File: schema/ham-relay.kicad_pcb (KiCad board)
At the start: 2 copper layers, 140 x 98 mm, 72 parts, among them J1 DB9, P1 JTAG, P2 CONN_01X08, P3 RESET, P4 ISP, P5 CONN_01X03, U1 REG3V3, U2 CPC1017N, U3 LPC1114FN28/102, U4 XYZ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

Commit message: Production ready
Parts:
- added HOLE2: 1pin, Connect:1pin, F.Cu at (183.3, 133.1)
- added HOLE2: 1pin, Connect:1pin, F.Cu at (75.3, 133.1)
- added HOLE2: 1pin, Connect:1pin, F.Cu at (75.3, 41.1)
- added HOLE2: 1pin, Connect:1pin, F.Cu at (183.3, 41.1)
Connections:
- J1 pad : (no net) -> GND
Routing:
- net GND: track 82.9 -> 97.2 mm
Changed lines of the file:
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@@
 (kicad_pcb (version 4) (host pcbnew 4.0.1-stable)
   (general
-    (links 163)
+    (links 169)
     (no_connects 0)
     (area 57.709999 38.024999 197.860001 136.175001)
     (thickness 1.6)
     (drawings 41)
-    (tracks 367)
+    (tracks 376)
     (zones 0)
-    (modules 72)
+    (modules 76)
     (nets 71)
   )
   (page A4)
   (layers
-    (0 F.Cu signal hide)
+    (0 F.Cu signal)
     (31 B.Cu signal)
     (32 B.Adhes user)
@@
     (mod_text_size 1 1)
     (mod_text_width 0.15)
-    (pad_size 3.35 3.35)
-    (pad_drill 3.048)
+    (pad_size 6 6)
+    (pad_drill 3.8)
     (pad_to_mask_clearance 0.2)
     (aux_axis_origin 69.342 125.222)
@@
     (add_net +12V)
   )
-  (module TO_SOT_Packages_THT:TO-220_Neutral123_Horizontal (layer F.Cu)
+  (module Connect:1pin (layer F.Cu)
+    (at 183.285 133.1)
+    (descr "module 1 pin (ou trou mecanique de percage)")
+    (tags DEV)
+    (zone_connect 2)
+    (fp_text reference HOLE2 (at 0 -3.048) (layer F.SilkS) hide
+      (effects (font (size 1 1) (thickness 0.15)))
+    )
+    (fp_text value 1pin (at 0 2.794) (layer F.Fab)
+      (effects (font (size 1 1) (thickness 0.15)))
+    )
+    (fp_circle (center 0 0) (end 0 -2.286) (layer F.SilkS) (width 0.15))
+    (pad 1 thru_hole circle (at 0 0) (size 6 6) (drill 3.8) (layers *.Cu *.Mask F.SilkS)
+      (net 1 GND) (zone_connect 2))
+  )
+  (module Connect:1pin (layer F.Cu)
+    (at 75.285 133.1)
+    (descr "module 1 pin (ou trou mecanique de percage)")
+    (tags DEV)
+    (zone_connect 2)
+    (fp_text reference HOLE2 (at 0 -3.048) (layer F.SilkS) hide
+      (effects (font (size 1 1) (thickness 0.15)))
+    )
+    (fp_text value 1pin (at 0 2.794) (layer F.Fab)
+      (effects (font (size 1 1) (thickness 0.15)))
+    )
+    (fp_circle (center 0 0) (end 0 -2.286) (layer F.SilkS) (width 0.15))
+    (pad 1 thru_hole circle (at 0 0) (size 6 6) (drill 3.8) (layers *.Cu *.Mask F.SilkS)
+      (net 1 GND) (zone_connect 2))
+  )
+  (module Connect:1pin (layer F.Cu)
+    (at 75.285 41.1)
+    (descr "module 1 pin (ou trou mecanique de percage)")
+    (tags DEV)
+    (zone_connect 2)
+    (fp_text reference HOLE2 (at 0 -3.048) (layer F.SilkS) hide
+      (effects (font (size 1 1) (thickness 0.15)))
+    )
+    (fp_text value 1pin (at 0 2.794) (layer F.Fab)
+      (effects (font (size 1 1) (thickness 0.15)))
+    )
+    (fp_circle (center 0 0) (end 0 -2.286) (layer F.SilkS) (width 0.15))
+    (pad 1 thru_hole circle (at 0 0) (size 6 6) (drill 3.8) (layers *.Cu *.Mask F.SilkS)
+      (net 1 GND) (zone_connect 2))
+  )
+  (module TO_SOT_Packages_THT:TO-220_Neutral123_Horizontal locked (layer F.Cu)
     (at 174.625 66.04 180)
     (descr "TO-220, Neutral, Horizontal,")
@@
     (fp_line (start 15.494 -10.414) (end -15.494 -10.414) (layer F.SilkS) (width 0.381))
     (fp_line (start -15.494 -10.414) (end -15.494 4.572) (layer F.SilkS) (width 0.381))
-    (pad "" thru_hole circle (at 12.49426 -7.112 270) (size 5.00126 5.00126) (drill 3.2004) (layers *.Cu *.Mask))
+    (pad "" thru_hole circle (at 12.49426 -7.112 270) (size 5.00126 5.00126) (drill 3.2004) (layers *.Cu *.Mask)
+      (net 1 GND))
     (pad 3 thru_hole oval (at 0 -8.382 270) (size 1.50114 1.99898) (drill 0.89916 (offset 0 -0.24892)) (layers *.Cu *.Mask)
       (net 3 /RX))
@@
     (pad 6 thru_hole oval (at 4.15544 -5.842 270) (size 1.50114 1.99898) (drill 0.89916 (offset 0 0.24892)) (layers *.Cu *.Mask)
       (net 23 /SWDIO))
-    (pad "" thru_hole circle (at -12.49426 -7.112 270) (size 5.00126 5.00126) (drill 3.2004) (layers *.Cu *.Mask))
+    (pad "" thru_hole circle (at -12.49426 -7.112 270) (size 5.00126 5.00126) (drill 3.2004) (layers *.Cu *.Mask)
+      (net 1 GND))
     (model walter/conn_d-sub/db_9f.wrl
       (at (xyz 0 0 0))
@@
     )
     (fp_circle (center 0 0) (end 0 -2.286) (layer F.SilkS) (width 0.15))
-    (pad 1 thru_hole circle (at 0 0) (size 4.064 4.064) (drill 3.048) (layers *.Cu *.Mask F.SilkS)
+    (pad 1 thru_hole circle (at 0 0) (size 4.5 4.5) (drill 3.5) (layers *.Cu *.Mask F.SilkS)
+      (net 1 GND) (zone_connect 2))
+  )
+  (module Connect:1pin (layer F.Cu)
+    (at 183.285 41.1)
+    (descr "module 1 pin (ou trou mecanique de percage)")
+    (tags DEV)
+    (zone_connect 2)
+    (fp_text reference HOLE2 (at 0 -3.048) (layer F.SilkS) hide
+      (effects (font (size 1 1) (thickness 0.15)))
+    )
+    (fp_text value 1pin (at 0 2.794) (layer F.Fab)
+      (effects (font (size 1 1) (thickness 0.15)))
+    )
+    (fp_circle (center 0 0) (end 0 -2.286) (layer F.SilkS) (width 0.15))
+    (pad 1 thru_hole circle (at 0 0) (size 6 6) (drill 3.8) (layers *.Cu *.Mask F.SilkS)
       (net 1 GND) (zone_connect 2))
   )
@@
     (effects (font (size 1 1) (thickness 0.15)))
   )
-  (gr_text STATUS (at 62.23 70.485 90) (layer F.SilkS)
+  (gr_text STATUS (at 62.23 70.358 90) (layer F.SilkS)
     (effects (font (size 1 1) (thickness 0.15)))
   )
-  (gr_text TONE (at 62.23 63.5 90) (layer F.SilkS)
+  (gr_text TONE (at 62.23 63.373 90) (layer F.SilkS)
     (effects (font (size 1 1) (thickness 0.15)))
   )
-  (gr_text TX (at 62.23 56.515 90) (layer F.SilkS)
+  (gr_text TX (at 62.23 56.388 90) (layer F.SilkS)
     (effects (font (size 1 1) (thickness 0.15)))
   )
-  (gr_text SQ (at 62.23 49.53 90) (layer F.SilkS)
+  (gr_text SQ (at 62.23 49.403 90) (layer F.SilkS)
     (effects (font (size 1 1) (thickness 0.15)))
   )
@@
   (gr_line (start 57.785 38.1) (end 197.785 38.1) (angle 90) (layer Edge.Cuts) (width 0.15))
   (gr_line (start 57.785 38.1) (end 57.785 136.1) (angle 90) (layer Edge.Cuts) (width 0.15))
+  (segment (start 183.285 133.1) (end 183.285 129.437) (width 0.508) (layer F.Cu) (net 1))
+  (segment (start 183.285 129.437) (end 183.261 129.413) (width 0.508) (layer F.Cu) (net 1))
+  (segment (start 183.285 41.1) (end 183.285 44.68) (width 0.508) (layer F.Cu) (net 1))
+  (segment (start 183.285 44.68) (end 183.261 44.704) (width 0.508) (layer F.Cu) (net 1))
+  (segment (start 75.285 41.1) (end 75.285 44.932) (width 0.508) (layer F.Cu) (net 1))
+  (segment (start 75.285 44.932) (end 75.311 44.958) (width 0.508) (layer F.Cu) (net 1))
+  (segment (start 75.285 133.1) (end 75.285 130.074) (width 0.508) (layer F.Cu) (net 1))
+  (segment (start 75.285 130.074) (end 75.311 130.048) (width 0.508) (layer F.Cu) (net 1))
   (segment (start 81.28 123.825) (end 81.28 111.76) (width 0.508) (layer B.Cu) (net 1))
   (via (at 81.28 111.76) (size 1.5) (drill 0.5) (layers F.Cu B.Cu) (net 1))
@@
   (via (at 189.865 57.15) (size 1.5) (drill 0.5) (layers F.Cu B.Cu) (net 22))
   (segment (start 189.865 57.15) (end 152.36 57.15) (width 0.508) (layer F.Cu) (net 22) (status 20))
+  (segment (start 63.5 106.68) (end 66.167 104.013) (width 0.508) (layer F.Cu) (net 23))
+  (segment (start 66.167 104.013) (end 75.692 104.013) (width 0.508) (layer F.Cu) (net 23))
+  (segment (start 75.692 104.013) (end 76.2 103.505) (width 0.508) (layer F.Cu) (net 23))
   (segment (start 80.01 84.455) (end 67.945 84.455) (width 0.508) (layer B.Cu) (net 23) (status 10))
   (via (at 63.5 106.68) (size 1.5) (drill 0.5) (layers F.Cu B.Cu) (net 23))
@@
   (segment (start 94.615 101.6) (end 96.52 99.695) (width 0.508) (layer F.Cu) (net 23) (status 20))
   (segment (start 77.47 101.6) (end 94.615 101.6) (width 0.508) (layer F.Cu) (net 23))
-  (segment (start 76.2 103.505) (end 66.675 103.505) (width 0.508) (layer F.Cu) (net 23) (status 10))
   (segment (start 62.23 114.935) (end 64.15044 116.85544) (width 0.508) (layer F.Cu) (net 23))
   (segment (start 62.23 107.95) (end 62.23 114.935) (width 0.508) (layer F.Cu) (net 23))
-  (segment (start 66.675 103.505) (end 63.5 106.68) (width 0.508) (layer F.Cu) (net 23))
   (segment (start 63.5 106.68) (end 62.23 107.95) (width 0.508) (layer F.Cu) (net 23))
   (segment (start 68.072 116.85544) (end 64.15044 116.85544) (width 0.508) (layer F.Cu) (net 23) (status 10))
@@
   (segment (start 126.492 115.443) (end 136.906 125.857) (width 0.508) (layer F.Cu) (net 52))
   (segment (start 193.675 119.38) (end 193.675 123.825) (width 0.508) (layer B.Cu) (net 53) (status 30))
-  (zone (net 0) (net_name "") (layer F.Cu) (hatch edge 0.508)
-    (connect_pads (clearance 0))
-    (min_thickness 0.254)
-    (keepout (tracks not_allowed) (vias not_allowed) (copperpour allowed))
-    (fill (arc_segments 16) (thermal_gap 0.508) (thermal_bridge_width 0.508))
-    (polygon
-      (pts
-        (xy 197.8 43.5) (xy 57.785 43.4848) (xy 57.785 38.1) (xy 197.8 38.1) (xy 197.8 43.5)
-      )
-    )
-  )
   (zone (net 0) (net_name "") (layer B.Cu) (hatch edge 0.508)
     (connect_pads (clearance 0))
     (min_thickness 0.254)
-    (keepout (tracks not_allowed) (vias not_allowed) (copperpour allowed))
-    (fill (arc_segments 16) (thermal_gap 0.508) (thermal_bridge_width 0.508))
-    (polygon
-      (pts
-        (xy 197.8 43.5) (xy 57.785 43.4848) (xy 57.785 38.1) (xy 197.8 38.1) (xy 197.8 43.5)
-      )
-    )
-  )
-  (zone (net 0) (net_name "") (layer B.Cu) (hatch edge 0.508)
-    (connect_pads (clearance 0))
-    (min_thickness 0.254)
-    (keepout (tracks not_allowed) (vias not_allowed) (copperpour allowed))
-    (fill (arc_segments 16) (thermal_gap 0.508) (thermal_bridge_width 0.508))
-    (polygon
-      (pts
-        (xy 197.8 136.1084) (xy 57.785 136.0932) (xy 57.785 130.7084) (xy 197.8 130.7084) (xy 197.8 136.1084)
-      )
-    )
-  )
-  (zone (net 0) (net_name "") (layer F.Cu) (hatch edge 0.508)
-    (connect_pads (clearance 0))
-    (min_thickness 0.254)

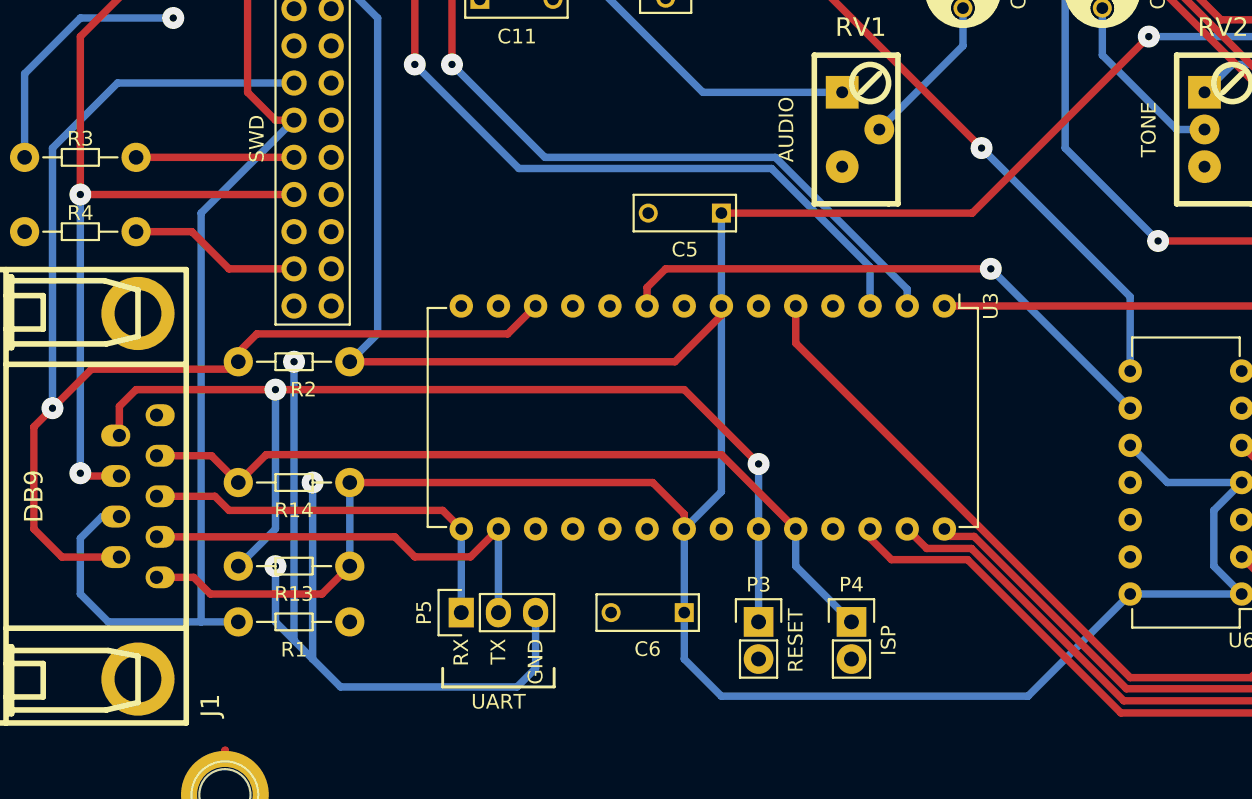
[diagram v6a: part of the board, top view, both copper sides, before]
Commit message: Start fixing schematics
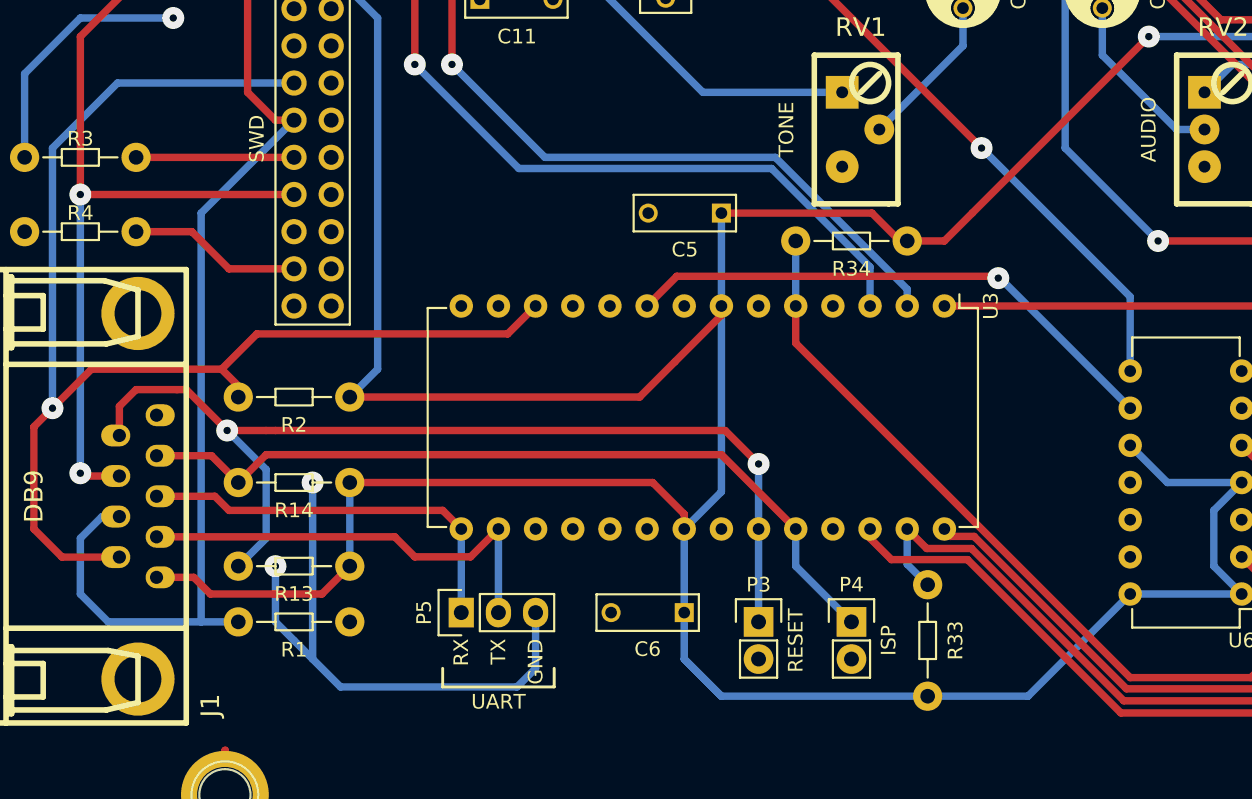
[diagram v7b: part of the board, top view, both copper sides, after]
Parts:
- added R33: 560k, resistors:Resistor_Horizontal_RM08mm, F.Cu at (123.3, 122.6)
- added R34: 560k, resistors:Resistor_Horizontal_RM08mm, F.Cu at (118.1, 95.2)
- D7: value RX -> EXT
- R10: value ? -> 560
- R12, R16: value ? -> 2k7
- R15: value ? -> 1k8
- R17: value 560 -> 270
- R18: value 560 -> 1k8
- R19: value 560 -> 330
- R27: value 220k -> 680k
- R28: value 220k -> 330k
- R32: value ? -> 15k
- R5: value ? -> 1k
- R8: value 560 -> 180
- R9: value ? -> 330
- U4, U5, U7: value XYZ -> MCA231
- moved R2 2.41 mm to (80.0, 105.9)
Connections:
- J1 pad : GND -> (no net)
- P1 pad 15: Net-(P1-Pad15) -> (no net)
- P1 pad 19: Net-(P1-Pad19) -> (no net)
- P1 pad 3: Net-(P1-Pad3) -> (no net)
- P1 pad 5: Net-(P1-Pad5) -> (no net)
- U1 pad 1: VCC -> (no net)
- U1 pad 2: GND -> (no net)
- U1 pad 3: +3V3 -> (no net)
- U3 pad 10: Net-(U3-Pad10) -> (no net)
- U3 pad 11: Net-(U3-Pad11) -> (no net)
- U3 pad 13: Net-(U3-Pad13) -> (no net)
- U3 pad 14: Net-(U3-Pad14) -> (no net)
- U3 pad 17: Net-(U3-Pad17) -> (no net)
- U3 pad 18: Net-(U3-Pad18) -> (no net)
- U3 pad 19: Net-(U3-Pad19) -> (no net)
- U3 pad 25: Net-(U3-Pad25) -> (no net)
- U3 pad 4: Net-(U3-Pad4) -> (no net)
- U3 pad 6: Net-(U3-Pad6) -> (no net)
- U4 pad 6: Net-(U4-Pad6) -> (no net)
- U5 pad 6: Net-(U5-Pad6) -> (no net)
- U7 pad 6: Net-(U7-Pad6) -> (no net)
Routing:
- net GND: track 97.2 -> 78.1 mm, vias 4 -> 3
- net +3V3: track 315.7 -> 324.3 mm
- net Net-(R34-Pad2): track 52.7 -> 57.1 mm
- net /RXE: track 59.7 -> 64.1 mm
- net /SWDIO: track 87.8 -> 89.8 mm
- net /RESET: track 72.2 -> 70.2 mm
- net Net-(U3-Pad9): track 39.4 -> 37.6 mm

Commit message: Update schematics after prototype validation
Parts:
- R33, R34: value 560k -> 56k
- U2: value CPC1017N -> LH1540
- moved R18 1.40 mm to (75.6, 67.8)
- moved R15 1.40 mm to (75.6, 46.9)
- moved R17 1.40 mm to (75.6, 53.8)
- moved R8 1.40 mm to (75.6, 60.8)
- moved D2 1.25 mm to (65.8, 63.4)
- moved D4 1.25 mm to (65.8, 49.4)
- moved D5 1.25 mm to (65.8, 56.4)
- moved D6 1.25 mm to (65.8, 70.4)
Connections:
- U2 pad 3: /Audio/TONE -> (no net)
- U2 pad 6: (no net) -> /Audio/TONE
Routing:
- net /Audio/TONE: track 76.8 -> 92.0 mm
- net /SWO: track 122.3 -> 123.2 mm
- net Net-(R18-Pad1): track 75.2 -> 75.8 mm
- net /TONE_SW: track 143.2 -> 142.6 mm
- net VCC: track 223.5 -> 222.9 mm
- net /TXE: track 133.8 -> 133.2 mm
- net /RX_CR: track 198.1 -> 197.6 mm
